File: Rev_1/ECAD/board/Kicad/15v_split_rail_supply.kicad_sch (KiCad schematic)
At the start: 18 parts, among them Q1 IPP029N15NM6, U1 LM3478MA

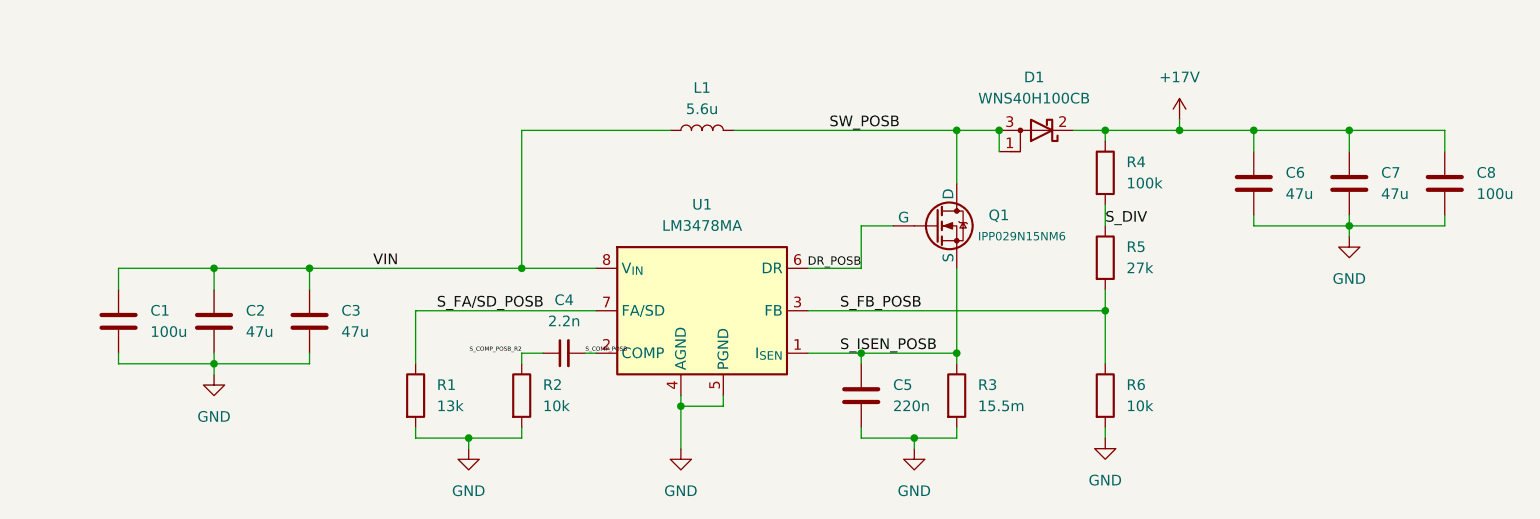
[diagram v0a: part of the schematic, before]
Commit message: Assigned footprint and 3d-models for +17V switch regulator
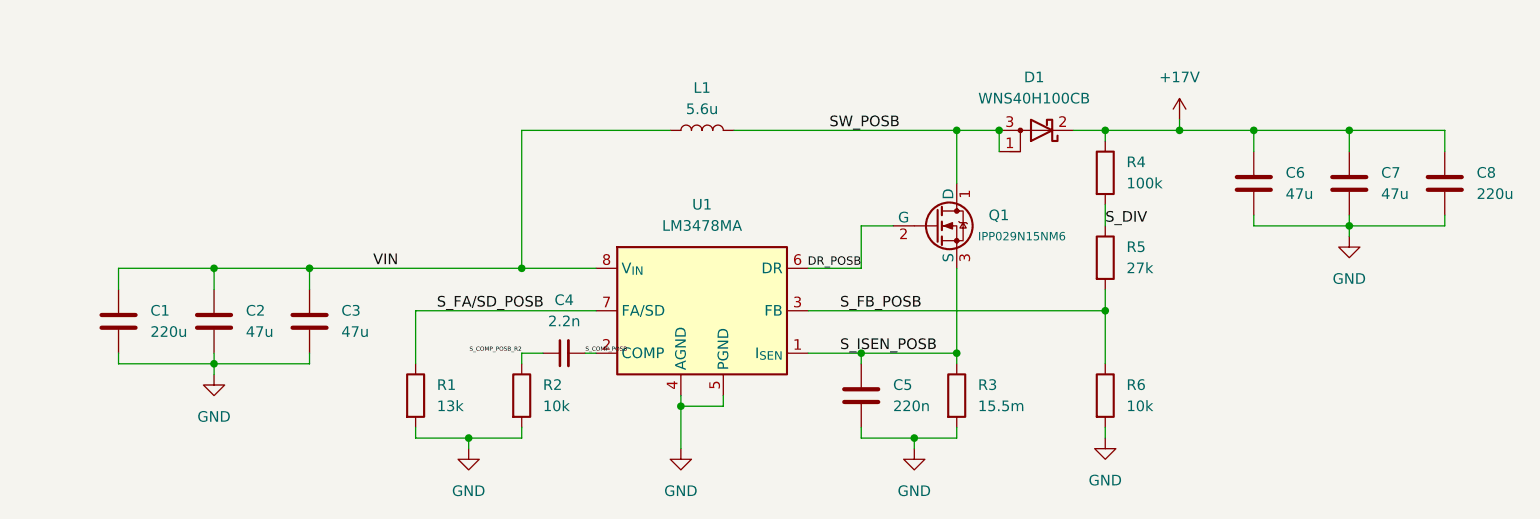
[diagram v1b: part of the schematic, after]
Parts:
- C1, C8: value 100u -> 220u; footprint Capacitor_SMD:C_0805_2012Metric_Pad1.18x1.45mm_HandSolder -> Capacitor_SMD:CP_Elec_10x10.5; Mouser NO: (none) -> 80-A768MS227M1GLAS22
- C2, C3, C6, C7: footprint Capacitor_SMD:C_0805_2012Metric_Pad1.18x1.45mm_HandSolder -> Capacitor_SMD:C_1210_3225Metric_Pad1.33x2.70mm_HandSolder; Mouser NO: (none) -> 810-C3216X5R1E476M
- D1: footprint (none) -> Package_TO_SOT_SMD:TO-263-3_TabPin2
- L1: footprint (none) -> filip:IHLP5050FD
- Q1: footprint (none) -> filip:PSMN4R0
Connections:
- net +3V3: no longer names the net of C6.1, C7.1, C8.1, D1.2 (K), R4.1
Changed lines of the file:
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@@
       (effects (font (size 1.27 1.27)) (justify left))
     )
-    (property "Footprint" "Capacitor_SMD:C_0805_2012Metric_Pad1.18x1.45mm_HandSolder" (at 220.6752 57.15 0)
+    (property "Footprint" "Capacitor_SMD:C_1210_3225Metric_Pad1.33x2.70mm_HandSolder" (at 220.6752 57.15 0)
       (effects (font (size 1.27 1.27)) hide)
     )
@@
       (effects (font (size 1.27 1.27)) hide)
     )
+    (property "Mouser NO:" "810-C3216X5R1E476M" (at 219.71 53.34 0)
+      (effects (font (size 1.27 1.27)) hide)
+    )
     (pin "1")
     (pin "2")
@@
       (effects (font (size 1.27 1.27)) (justify left))
     )
-    (property "Footprint" "Capacitor_SMD:C_0805_2012Metric_Pad1.18x1.45mm_HandSolder" (at 96.2152 73.66 0)
+    (property "Footprint" "Capacitor_SMD:C_1210_3225Metric_Pad1.33x2.70mm_HandSolder" (at 96.2152 73.66 0)
       (effects (font (size 1.27 1.27)) hide)
     )
@@
       (effects (font (size 1.27 1.27)) hide)
     )
+    (property "Mouser NO:" "810-C3216X5R1E476M" (at 95.25 69.85 0)
+      (effects (font (size 1.27 1.27)) hide)
+    )
     (pin "1")
     (pin "2")
@@
     )
     (property "Datasheet" "https://www.ti.com/lit/gpn/lm3478" (at 142.875 55.88 0)
+      (effects (font (size 1.27 1.27)) hide)
+    )
+    (property "Mouser NO:" "" (at 142.24 68.58 0)
       (effects (font (size 1.27 1.27)) hide)
     )
@@
       (effects (font (size 1.27 1.27)) hide)
     )
+    (property "Mouser NO:" "" (at 190.5 62.23 0)
+      (effects (font (size 1.27 1.27)) hide)
+    )
     (pin "1")
     (pin "2")
@@
       (effects (font (size 1.27 1.27)) hide)
     )
+    (property "Mouser NO:" "" (at 107.95 78.74 0)
+      (effects (font (size 1.27 1.27)) hide)
+    )
     (pin "1")
     (pin "2")
@@
       (effects (font (size 1.27 1.27)) hide)
     )
+    (property "Mouser NO:" "" (at 190.5 78.74 0)
+      (effects (font (size 1.27 1.27)) hide)
+    )
     (pin "1")
     (pin "2")
@@
       (effects (font (size 1.27 1.27)))
     )
-    (property "Footprint" "" (at 182.88 46.99 0)
+    (property "Footprint" "Package_TO_SOT_SMD:TO-263-3_TabPin2" (at 182.88 46.99 0)
       (effects (font (size 1.27 1.27)) hide)
     )
@@
       (effects (font (size 1.27 1.27)) hide)
     )
+    (property "Mouser NO:" "" (at 182.88 46.99 0)
+      (effects (font (size 1.27 1.27)) hide)
+    )
     (pin "1")
     (pin "2")
@@
       (effects (font (size 1.27 1.27)) (justify left))
     )
-    (property "Footprint" "Capacitor_SMD:C_0805_2012Metric_Pad1.18x1.45mm_HandSolder" (at 84.7852 73.66 0)
+    (property "Footprint" "Capacitor_SMD:C_1210_3225Metric_Pad1.33x2.70mm_HandSolder" (at 84.7852 73.66 0)
       (effects (font (size 1.27 1.27)) hide)
     )
@@
       (effects (font (size 1.27 1.27)) hide)
     )
+    (property "Mouser NO:" "810-C3216X5R1E476M" (at 83.82 69.85 0)
+      (effects (font (size 1.27 1.27)) hide)
+    )
     (pin "1")
     (pin "2")
@@
       (effects (font (size 1.27 1.27)) hide)
     )
+    (property "Mouser NO:" "" (at 120.65 78.74 0)
+      (effects (font (size 1.27 1.27)) hide)
+    )
     (pin "1")
     (pin "2")
@@
       (effects (font (size 1.27 1.27)) hide)
     )
+    (property "Mouser NO:" "" (at 190.5 52.07 0)
+      (effects (font (size 1.27 1.27)) hide)
+    )
     (pin "1")
     (pin "2")
@@
       (effects (font (size 1.27 1.27)) hide)
     )
+    (property "Mouser NO:" "" (at 125.73 73.66 0)
+      (effects (font (size 1.27 1.27)) hide)
+    )
     (pin "1")
     (pin "2")
@@
     )
     (property "Datasheet" "~" (at 172.72 78.74 0)
+      (effects (font (size 1.27 1.27)) hide)
+    )
+    (property "Mouser NO:" "" (at 172.72 78.74 0)
       (effects (font (size 1.27 1.27)) hide)
     )
@@
       (effects (font (size 1 1)) (justify left))
     )
-    (property "Footprint" "" (at 175.26 55.88 0)
-      (effects (font (size 1.27 1.27)) hide)
-    )
-    (property "Datasheet" "https://eu.mouser.com/datasheet/2/196/Infineon_IPP029N15NM6_DataSheet_v02_00_EN-3478353.pdf" (at 170.18 71.12 0)
+    (property "Footprint" "filip:PSMN4R0" (at 175.26 55.88 0)
+      (effects (font (size 1.27 1.27)) hide)
+    )
+    (property "Datasheet" "https://assets.nexperia.com/documents/data-sheet/PSMN4R0-30YLD.pdf" (at 170.18 71.12 0)
       (effects (font (size 1.27 1.27)) hide)
     )
@@
       (effects (font (size 1.27 1.27)) hide)
     )
+    (property "Mouser NO:" "" (at 170.18 58.42 0)
+      (effects (font (size 1.27 1.27)) hide)
+    )
     (pin "1")
     (pin "2")
@@
       (effects (font (size 1.27 1.27)) hide)
     )
+    (property "Mouser NO:" "" (at 161.29 78.74 0)
+      (effects (font (size 1.27 1.27)) hide)
+    )
     (pin "1")
     (pin "2")
@@
       (effects (font (size 1.27 1.27)))
     )
-    (property "Footprint" "" (at 142.24 46.99 0)
+    (property "Footprint" "filip:IHLP5050FD" (at 142.24 46.99 0)
       (effects (font (size 1.27 1.27)) hide)
     )
@@
       (effects (font (size 1.27 1.27)) hide)
     )
+    (property "Mouser NO:" "" (at 142.24 46.99 0)
+      (effects (font (size 1.27 1.27)) hide)
+    )
     (pin "1")
     (pin "2")
@@
       (effects (font (size 1.27 1.27)) (justify left))
     )
-    (property "Value" "100u" (at 234.95 54.61 0)
-      (effects (font (size 1.27 1.27)) (justify left))
-    )
-    (property "Footprint" "Capacitor_SMD:C_0805_2012Metric_Pad1.18x1.45mm_HandSolder" (at 232.1052 57.15 0)
-      (effects (font (size 1.27 1.27)) hide)
-    )
-    (property "Datasheet" "~" (at 231.14 53.34 0)
+    (property "Value" "220u" (at 234.95 54.61 0)
+      (effects (font (size 1.27 1.27)) (justify left))
+    )
+    (property "Footprint" "Capacitor_SMD:CP_Elec_10x10.5" (at 232.1052 57.15 0)
+      (effects (font (size 1.27 1.27)) hide)
+    )
+    (property "Datasheet" "https://eu.mouser.com/datasheet/2/447/KEM_A4088_A768-3316438.pdf" (at 231.14 53.34 0)
+      (effects (font (size 1.27 1.27)) hide)
+    )
+    (property "Mouser NO:" "80-A768MS227M1GLAS22" (at 231.14 53.34 0)
       (effects (font (size 1.27 1.27)) hide)
     )
@@
       (effects (font (size 1.27 1.27)) (justify left))
     )
-    (property "Value" "100u" (at 76.2 71.12 0)
-      (effects (font (size 1.27 1.27)) (justify left))
-    )
-    (property "Footprint" "Capacitor_SMD:C_0805_2012Metric_Pad1.18x1.45mm_HandSolder" (at 73.3552 73.66 0)
-      (effects (font (size 1.27 1.27)) hide)
-    )
-    (property "Datasheet" "~" (at 72.39 69.85 0)
+    (property "Value" "220u" (at 76.2 71.12 0)
+      (effects (font (size 1.27 1.27)) (justify left))
+    )
+    (property "Footprint" "Capacitor_SMD:CP_Elec_10x10.5" (at 73.3552 73.66 0)
+      (effects (font (size 1.27 1.27)) hide)
+    )
+    (property "Datasheet" "https://eu.mouser.com/datasheet/2/447/KEM_A4088_A768-3316438.pdf" (at 72.39 69.85 0)
+      (effects (font (size 1.27 1.27)) hide)
+    )
+    (property "Mouser NO:" "80-A768MS227M1GLAS22" (at 72.39 69.85 0)
       (effects (font (size 1.27 1.27)) hide)
     )
@@
       (effects (font (size 1.27 1.27)) (justify left))
     )
-    (property "Footprint" "Capacitor_SMD:C_0805_2012Metric_Pad1.18x1.45mm_HandSolder" (at 209.2452 57.15 0)
+    (property "Footprint" "Capacitor_SMD:C_1210_3225Metric_Pad1.33x2.70mm_HandSolder" (at 209.2452 57.15 0)
       (effects (font (size 1.27 1.27)) hide)
     )
@@
       (effects (font (size 1.27 1.27)) hide)
     )
+    (property "Mouser NO:" "810-C3216X5R1E476M" (at 208.28 53.34 0)
+      (effects (font (size 1.27 1.27)) hide)
+    )

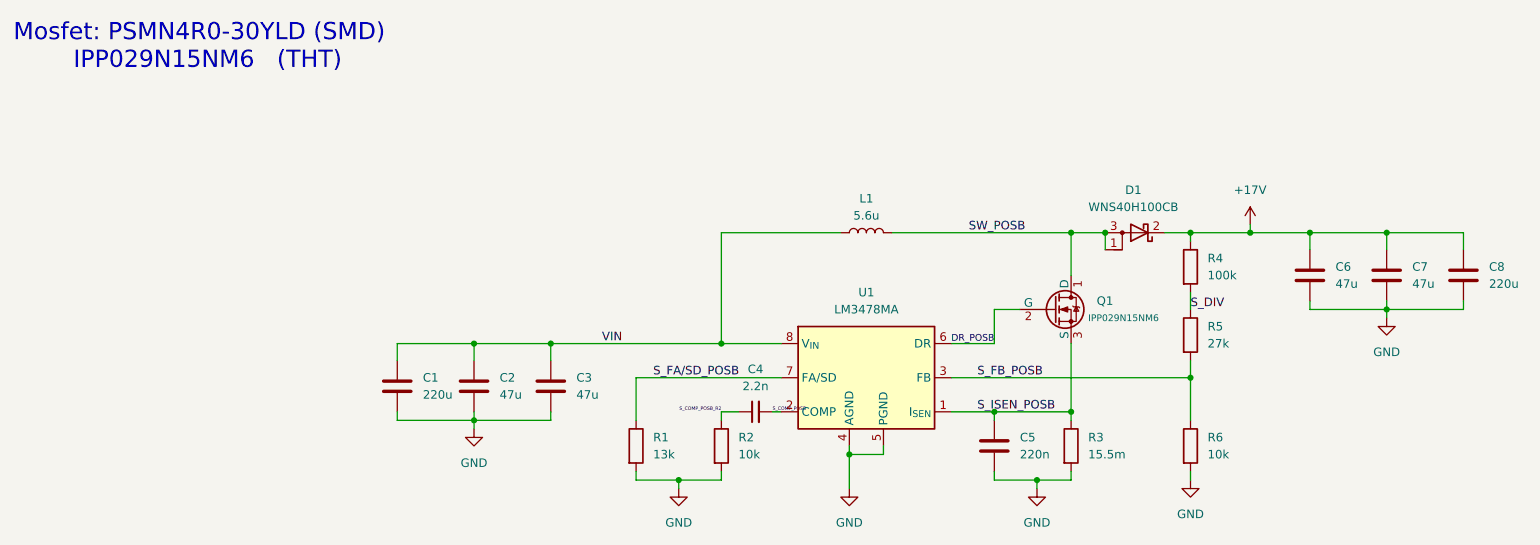
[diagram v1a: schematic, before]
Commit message: Made the logic for Overcurrent
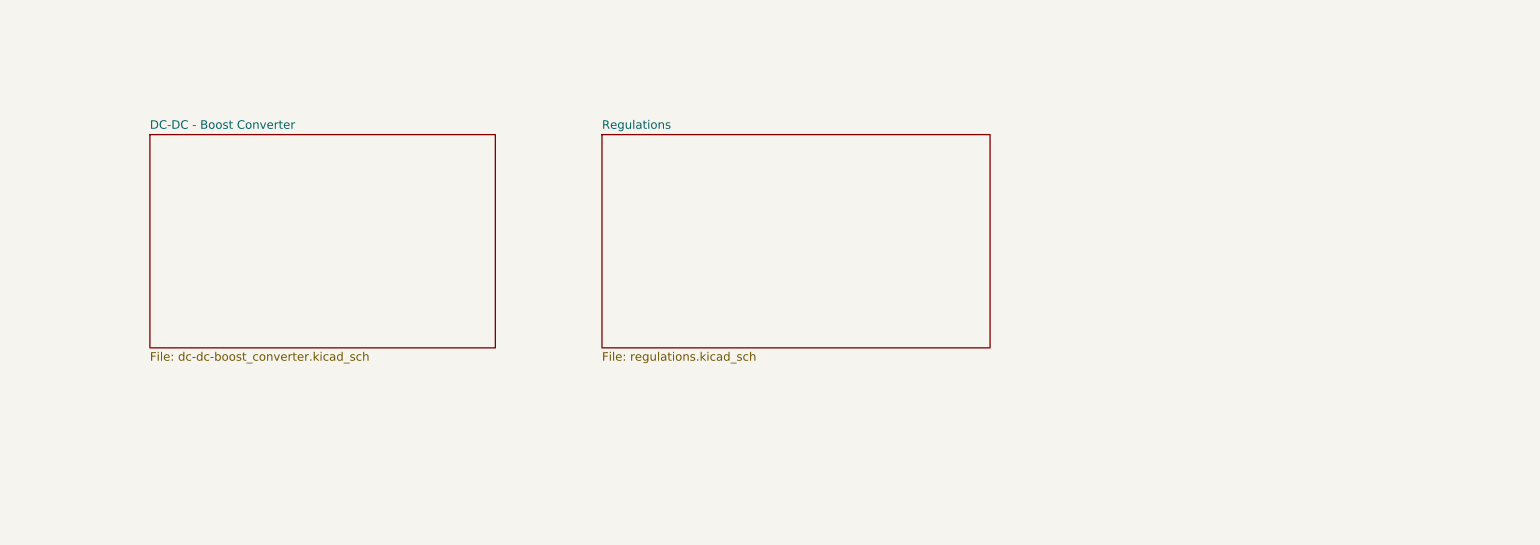
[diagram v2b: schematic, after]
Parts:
- removed C1, C8: 220u, Capacitor_SMD:CP_Elec_10x10.5, symbol Device:C
- removed C2, C3, C6, C7: 47u, Capacitor_SMD:C_1210_3225Metric_Pad1.33x2.70mm_HandSolder, symbol Device:C
- removed C4: 2.2n, Capacitor_SMD:C_0805_2012Metric_Pad1.18x1.45mm_HandSolder, symbol Device:C_Small
- removed C5: 220n, Capacitor_SMD:C_0805_2012Metric_Pad1.18x1.45mm_HandSolder, symbol Device:C
- removed D1: WNS40H100CB, Package_TO_SOT_SMD:TO-263-3_TabPin2, symbol Device:D_Schottky_AKA
- removed L1: 5.6u, filip:IHLP5050FD, symbol Device:L
- removed Q1: IPP029N15NM6, filip:PSMN4R0, symbol Simulation_SPICE:NMOS
- removed R1: 13k, Resistor_SMD:R_0805_2012Metric_Pad1.20x1.40mm_HandSolder, symbol Device:R
- removed R2, R6: 10k, Resistor_SMD:R_0805_2012Metric_Pad1.20x1.40mm_HandSolder, symbol Device:R
- removed R3: 15.5m, Resistor_SMD:R_1206_3216Metric_Pad1.30x1.75mm_HandSolder, symbol Device:R
- removed R4: 100k, Resistor_SMD:R_0805_2012Metric_Pad1.20x1.40mm_HandSolder, symbol Device:R
- removed R5: 27k, Resistor_SMD:R_0805_2012Metric_Pad1.20x1.40mm_HandSolder, symbol Device:R
- removed U1: LM3478MA, Package_SO:SOIC-8_3.9x4.9mm_P1.27mm, symbol Regulator_Controller:LM3478MA
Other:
- added sheet DC-DC - Boost Converter (dc-dc-boost_converter.kicad_sch)
- added sheet Regulations (regulations.kicad_sch)
- note removed: "Mosfet: PSMN4R0-30YLD (SMD) IPP029N15NM6 (THT)"

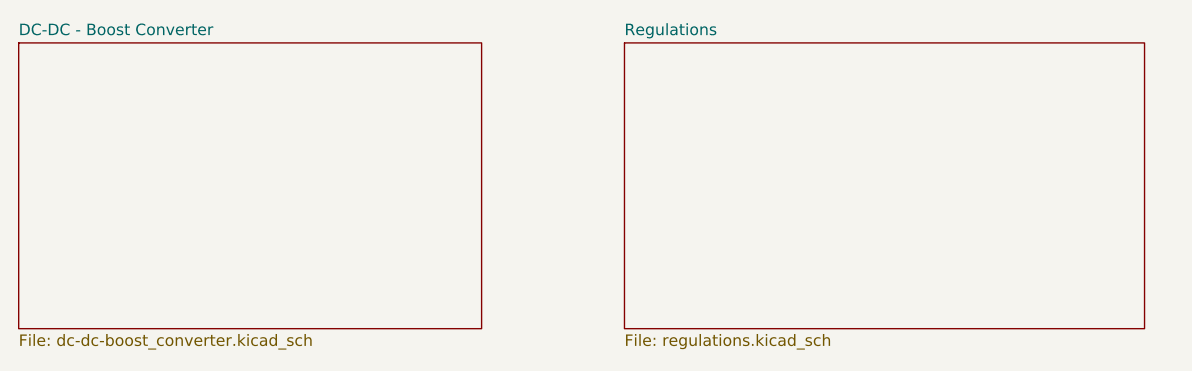
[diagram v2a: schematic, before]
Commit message: Components for 15V regulator are placed
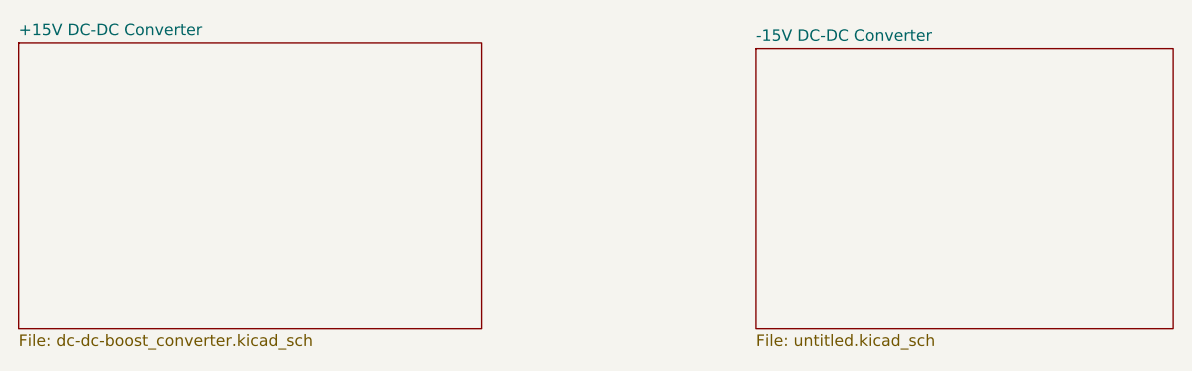
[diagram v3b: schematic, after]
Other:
- sheet DC-DC - Boost Converter renamed +15V DC-DC Converter
- removed sheet Regulations
- added sheet -15V DC-DC Converter (untitled.kicad_sch)
